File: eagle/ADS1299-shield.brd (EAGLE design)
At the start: 101.6 x 53.3 mm, 136 parts, among them IC1 ADS1299IPAG, IC2 TPS72325DBVT, IC3 TPS73225DBVT, IC5 24AA256UID, IC6 TPS604XXDBV, IC7 OPA376DBV, IC8 OPA376DBV, IC9 TXS0102DCTR, J16 EXTERNAL_SYNC, J8 Electrode Connector, U2 TXB0108PWR, U3 TXB0108PWR

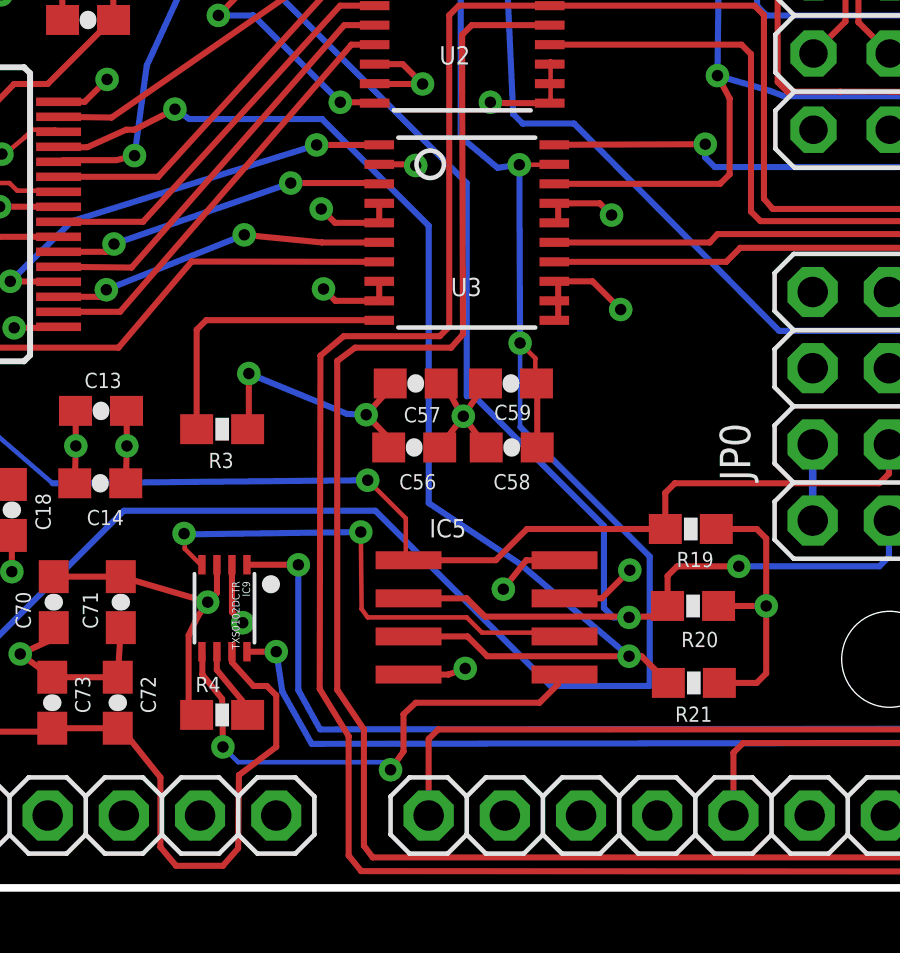
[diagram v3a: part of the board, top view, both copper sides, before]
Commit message: minor clearance and legend improvements
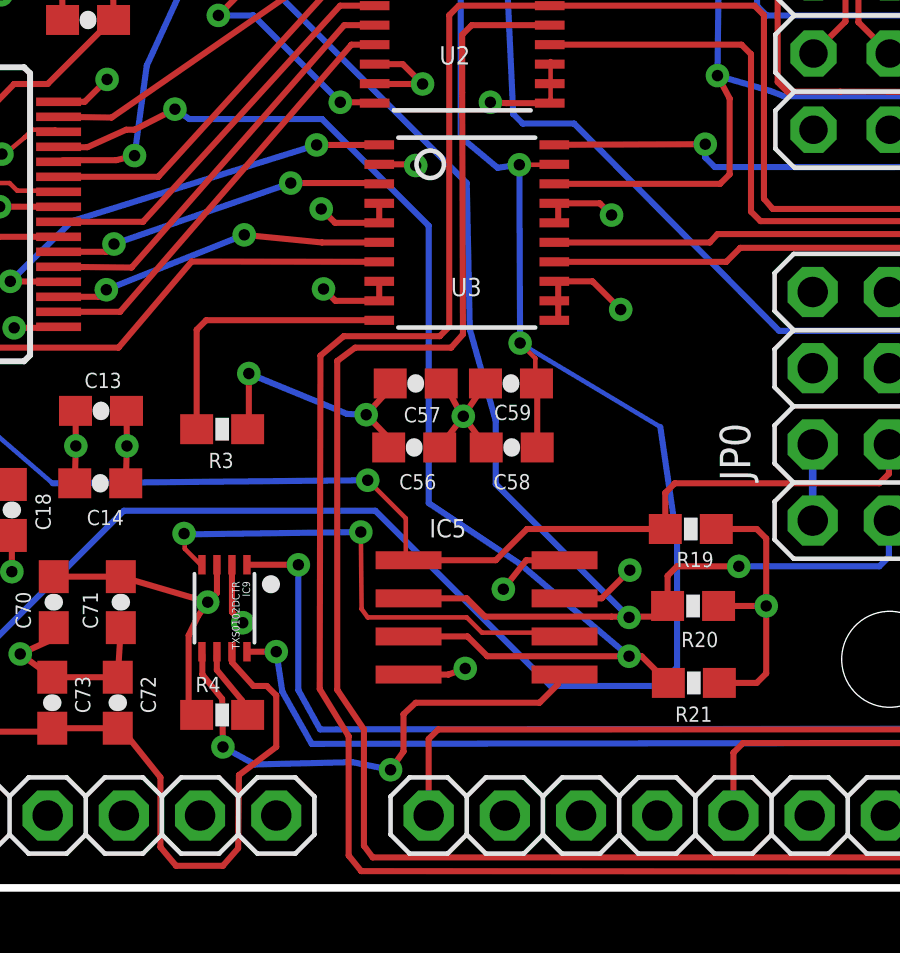
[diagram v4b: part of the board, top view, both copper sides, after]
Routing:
- net IOREF: track 102.5 -> 103.9 mm
- net BOARD_ADDR_1: track 57.1 -> 56.4 mm
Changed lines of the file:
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@@
 <grid distance="4" unitdist="mil" unit="mil" style="lines" multiple="1" display="yes" altdistance="0.001" altunitdist="inch" altunit="inch"/>
 <layers>
-<layer number="1" name="Top" color="4" fill="1" visible="no" active="yes"/>
+<layer number="1" name="Top" color="4" fill="1" visible="yes" active="yes"/>
 <layer number="2" name="AGND" color="3" fill="1" visible="no" active="yes"/>
 <layer number="3" name="Route3" color="4" fill="3" visible="no" active="no"/>
@@
 <wire x1="60.7568" y1="16.256" x2="62.6872" y2="16.256" width="0.254" layer="51"/>
 <wire x1="60.7568" y1="16.256" x2="60.7568" y2="16.764" width="0.254" layer="51"/>
+<text x="63.7794" y="22.1996" size="0.8128" layer="51" rot="R90">A</text>
+<text x="66.6496" y="22.225" size="0.8128" layer="51" rot="R90">B</text>
 </plain>
 <attributes>
@@
 <wire x1="38.1" y1="5.334" x2="33.274" y2="5.334" width="0.2032" layer="1"/>
 <wire x1="38.1" y1="5.334" x2="38.2524" y2="5.4492" width="0.1524" layer="1"/>
-<wire x1="53.848" y1="15.494" x2="53.848" y2="18.288" width="0.1524" layer="16"/>
-<wire x1="58.166" y1="11.176" x2="53.848" y2="15.494" width="0.2032" layer="16"/>
-<wire x1="58.166" y1="6.858" x2="58.166" y2="11.176" width="0.2032" layer="16"/>
-<wire x1="54.864" y1="6.858" x2="58.166" y2="6.858" width="0.2032" layer="16"/>
+<wire x1="58.5216" y1="15.494" x2="53.848" y2="18.288" width="0.1524" layer="16"/>
+<wire x1="59.0804" y1="11.684" x2="58.5216" y2="15.494" width="0.2032" layer="16"/>
+<wire x1="54.864" y1="6.858" x2="58.4581" y2="6.858" width="0.2032" layer="16"/>
+<wire x1="58.4581" y1="6.858" x2="59.0804" y2="7.4803" width="0.2032" layer="16"/>
+<wire x1="59.0804" y1="7.4803" x2="59.0804" y2="11.684" width="0.2032" layer="16"/>
 <wire x1="49.022" y1="12.7" x2="54.864" y2="6.858" width="0.2032" layer="16"/>
 <wire x1="40.64" y1="12.7" x2="49.022" y2="12.7" width="0.2032" layer="16"/>
@@
 <wire x1="45.72" y1="29.972" x2="42.5196" y2="29.972" width="0.2032" layer="16"/>
 <wire x1="52.07" y1="23.622" x2="45.72" y2="29.972" width="0.2032" layer="16"/>
-<wire x1="52.07" y1="16.51" x2="52.07" y2="23.622" width="0.2032" layer="16"/>
-<wire x1="52.324" y1="16.51" x2="52.07" y2="16.51" width="0.1524" layer="16"/>
-<wire x1="56.642" y1="12.192" x2="52.324" y2="16.51" width="0.2032" layer="16"/>
-<wire x1="57.4802" y1="9.144" x2="56.9595" y2="9.144" width="0.2032" layer="16"/>
-<wire x1="56.9595" y1="9.144" x2="56.642" y2="9.4615" width="0.2032" layer="16"/>
-<wire x1="56.642" y1="9.4615" x2="56.642" y2="12.192" width="0.2032" layer="16"/>
+<wire x1="52.1716" y1="18.7452" x2="52.07" y2="23.622" width="0.2032" layer="16"/>
+<wire x1="53.0352" y1="15.6972" x2="52.1716" y2="18.7452" width="0.2032" layer="16"/>
 <wire x1="38.608" y1="24.384" x2="38.4636" y2="24.3306" width="0.1524" layer="1"/>
 <wire x1="57.4802" y1="9.144" x2="56.896" y2="9.1694" width="0.1524" layer="1"/>
 <via x="40.9956" y="24.5364" extent="1-16" drill="0.381"/>
 <via x="57.4802" y="9.144" extent="1-16" drill="0.381"/>
+<wire x1="53.0352" y1="15.6972" x2="53.0352" y2="13.589" width="0.2032" layer="16"/>
+<wire x1="53.0352" y1="13.589" x2="57.4802" y2="9.144" width="0.2032" layer="16"/>
 </signal>
 <signal name="BOARD_ADDR_0">
@@
 <wire x1="43.9166" y1="6.4262" x2="43.2562" y2="7.239" width="0.2032" layer="1"/>
 <wire x1="43.942" y1="4.826" x2="43.9166" y2="6.4262" width="0.2032" layer="1"/>
-<wire x1="44.45" y1="4.318" x2="43.942" y2="4.826" width="0.1524" layer="16"/>
-<wire x1="49.276" y1="4.318" x2="44.45" y2="4.318" width="0.1524" layer="16"/>
-<wire x1="49.53" y1="4.064" x2="49.276" y2="4.318" width="0.1524" layer="16"/>
+<wire x1="45.0088" y1="4.2418" x2="43.942" y2="4.826" width="0.2032" layer="16"/>
+<wire x1="48.26" y1="4.318" x2="45.0088" y2="4.2418" width="0.2032" layer="16"/>
+<wire x1="49.53" y1="4.064" x2="48.26" y2="4.318" width="0.2032" layer="16"/>
 <wire x1="49.9618" y1="4.6736" x2="49.53" y2="4.064" width="0.2032" layer="1"/>
 <wire x1="49.9618" y1="5.9182" x2="49.9618" y2="4.6736" width="0.2032" layer="1"/>

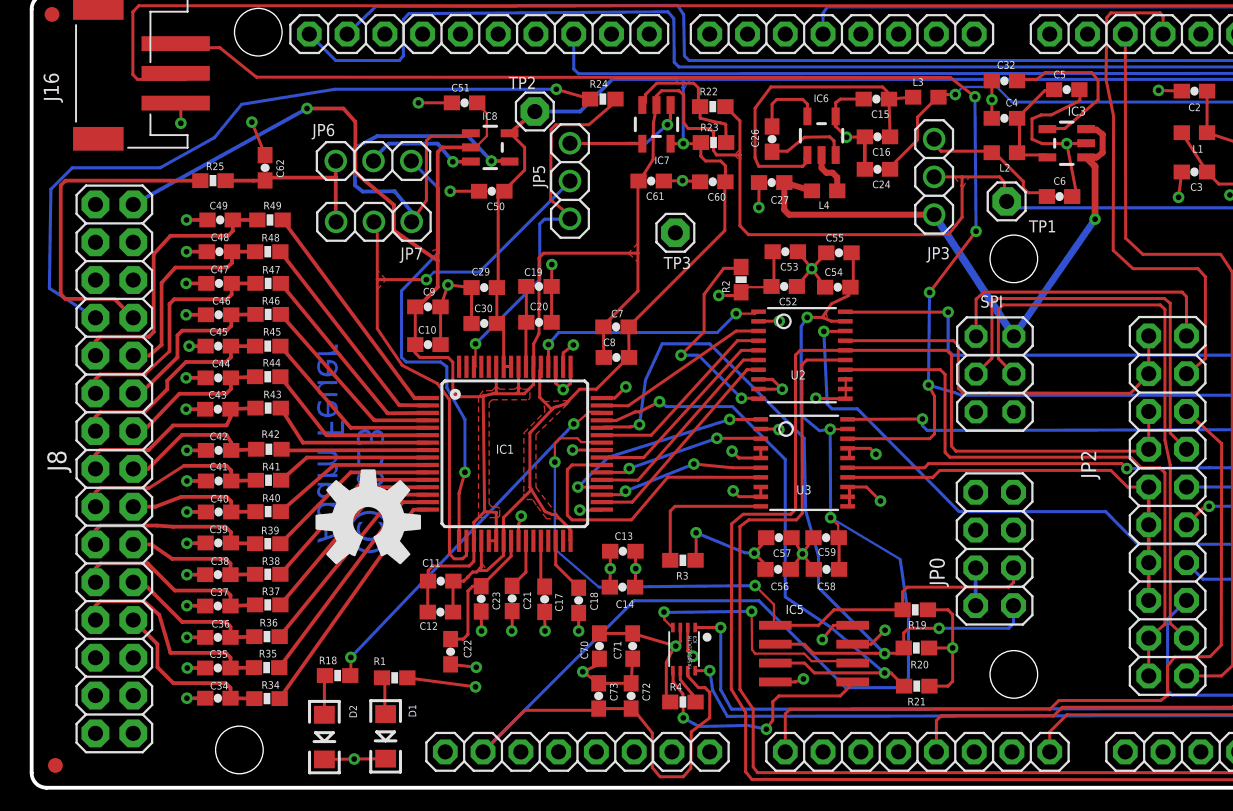
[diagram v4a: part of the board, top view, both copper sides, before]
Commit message: minor clearance and legend improvements
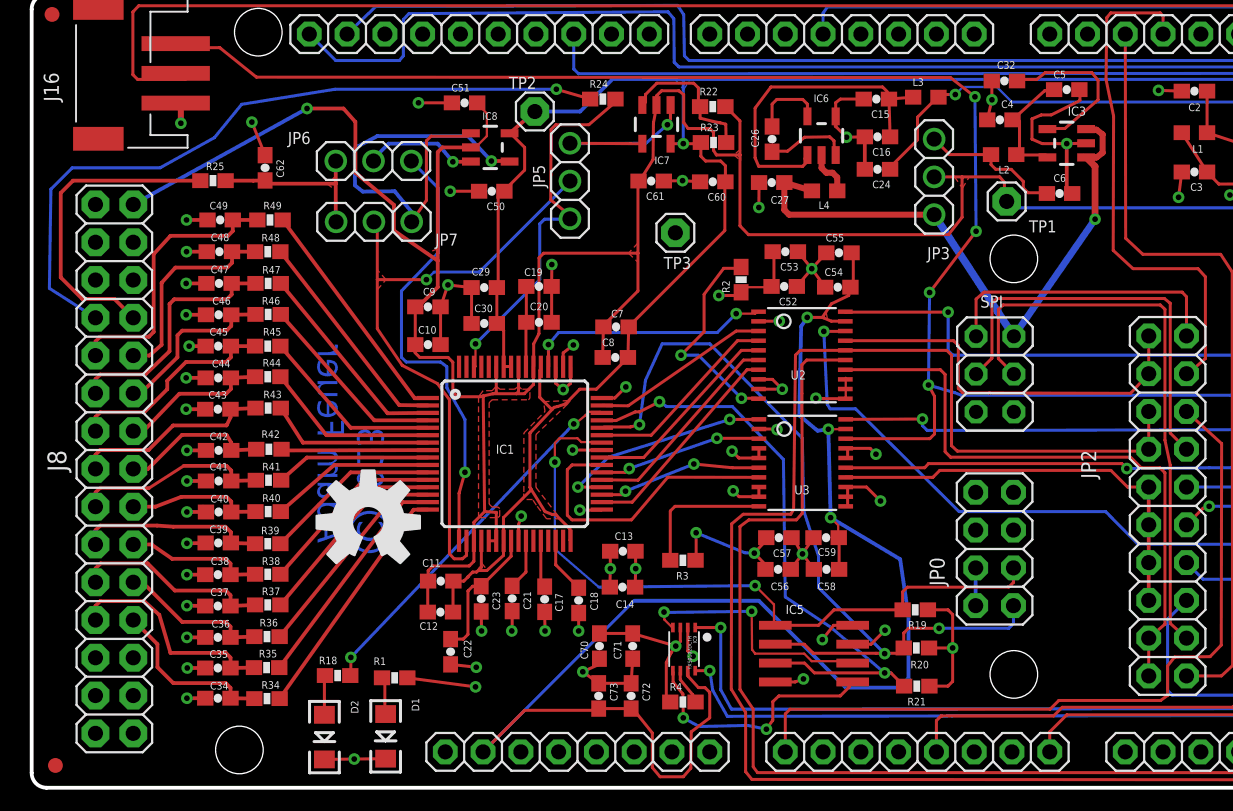
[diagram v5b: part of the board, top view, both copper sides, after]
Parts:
- moved C4 0.32 mm to (65.2, 45.0)
- moved C6 0.20 mm to (69.2, 40.1)
- moved L2 0.14 mm to (65.5, 42.7)
- moved U3 0.13 mm to (51.9, 22.0)
- moved C8 0.08 mm to (39.4, 29.1)
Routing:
- net REF_ELEC_CON: track 22.7 -> 21.7 mm
- added copper zone on layer 1, net REF_ELEC
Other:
- board text added: "GPIO4"
- board text added: "Power"

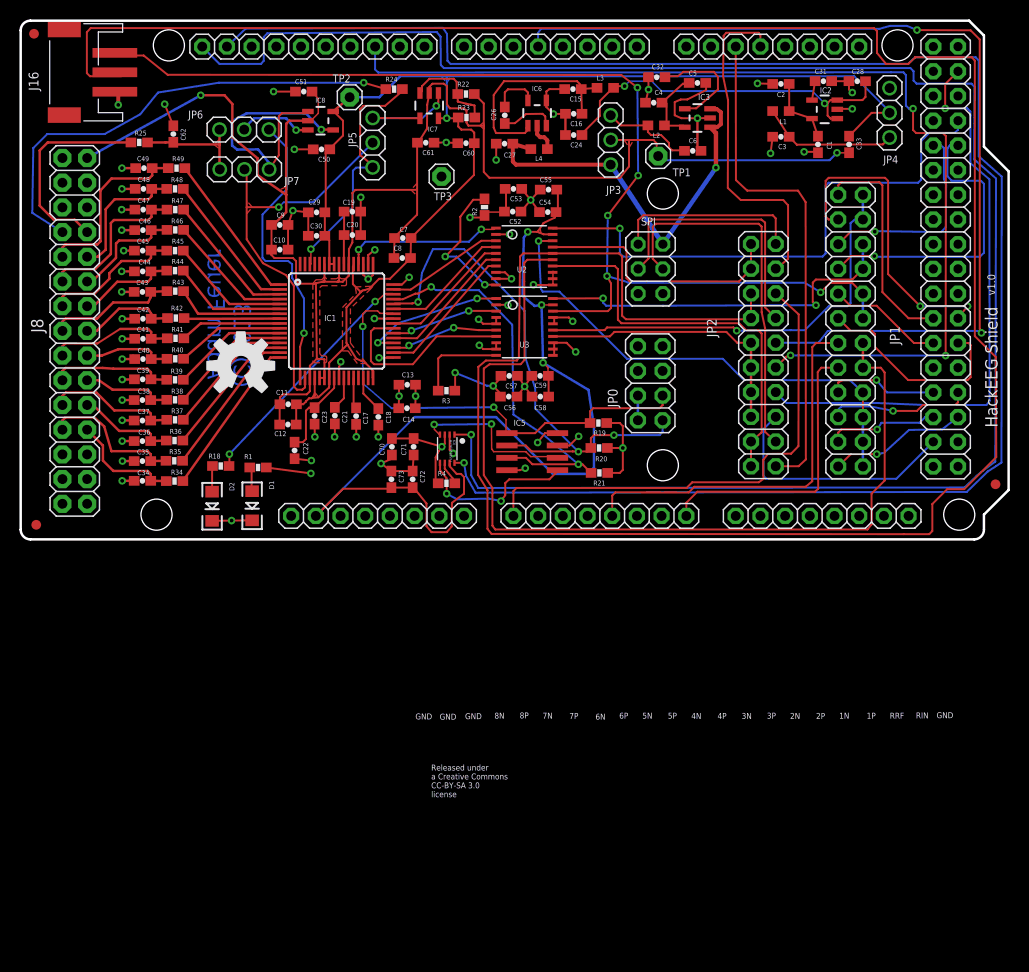
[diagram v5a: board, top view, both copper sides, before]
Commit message: updated silkscreen top and bottom for clarity; updated cam job to match
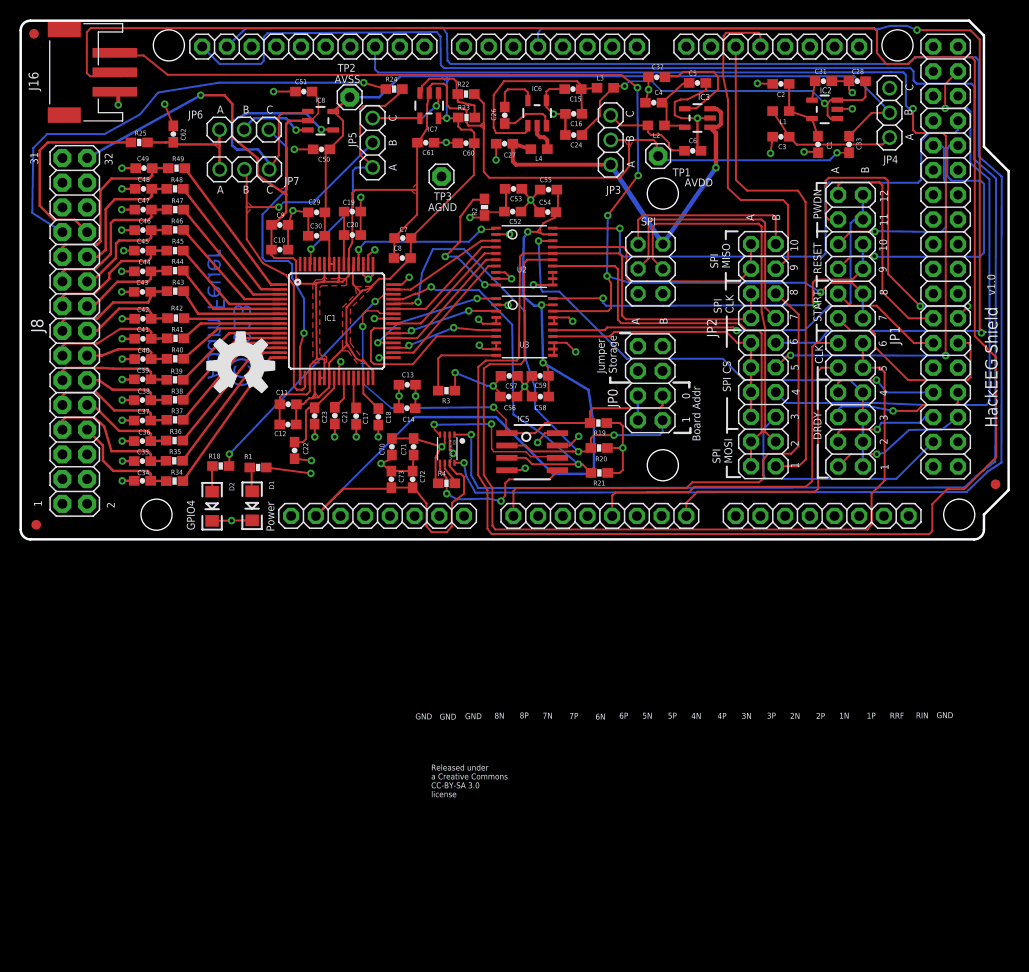
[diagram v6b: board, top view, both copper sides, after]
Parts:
- moved U$3 47.1 mm to (39.4, 12.1)
- moved U$4 11.3 mm to (33.7, 22.9)
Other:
- board text added: "AGND"
- board text added: "AVDD"
- board text added: "AVSS"
- board text added: "Released under a Creative Commons Attribution-ShareAlike 3.0 Unported (CC BY-SA 3.0) license"
